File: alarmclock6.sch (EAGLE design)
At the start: 47 parts, among them Q1 FDN360P, T1 2N2222, X1 MKDSN1,5/2-5,08, X2 MKDSN1,5/2-5,08, X3 MKDSN1,5/2-5,08, X4 MKDSN1,5/2-5,08

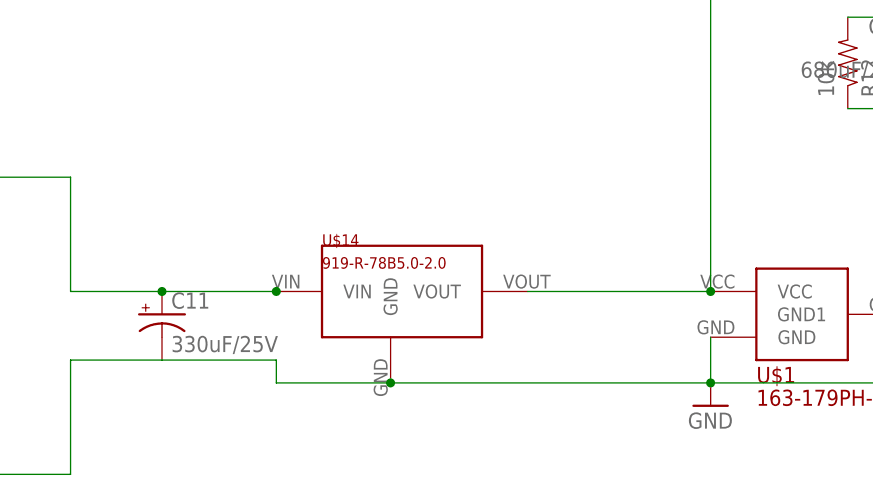
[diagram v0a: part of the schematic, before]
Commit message: bugfix on DC-DC converter
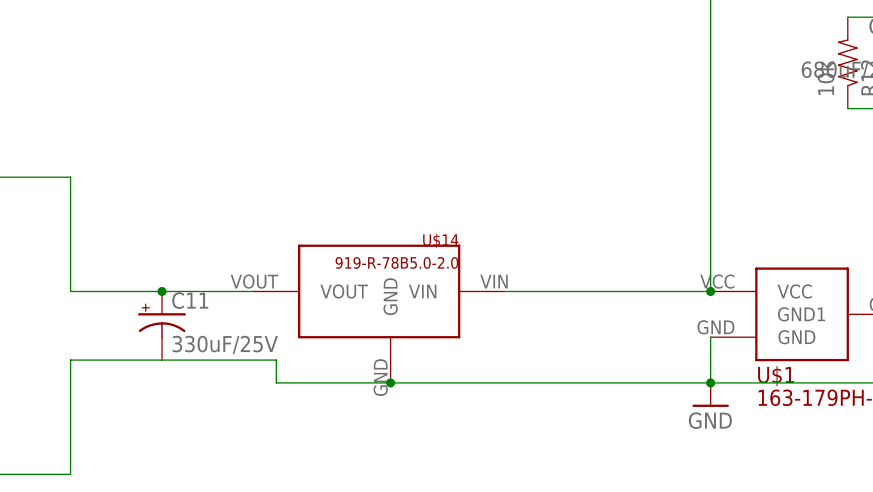
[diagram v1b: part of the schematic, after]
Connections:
- net N$3: now also U$14.VOUT; no longer U$14.VIN
- net N$43: now also U$14.VIN; no longer U$14.VOUT
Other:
- moved on the sheet: U$14
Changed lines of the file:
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@@
 <instance part="C18" gate="G$1" x="114.3" y="48.26"/>
 <instance part="C19" gate="G$1" x="119.38" y="48.26"/>
-<instance part="U$14" gate="G$1" x="-137.16" y="-129.54"/>
+<instance part="U$14" gate="G$1" x="-137.16" y="-129.54" rot="MR0"/>
 </instances>
 <busses>
@@
 <wire x1="-172.72" y1="-129.54" x2="-162.56" y2="-129.54" width="0.1524" layer="91"/>
 <pinref part="U$4" gate="G$1" pin="VCC"/>
-<wire x1="-162.56" y1="-129.54" x2="-149.86" y2="-129.54" width="0.1524" layer="91"/>
 <wire x1="-200.66" y1="-124.46" x2="-200.66" y2="-116.84" width="0.1524" layer="91"/>
 <wire x1="-200.66" y1="-116.84" x2="-172.72" y2="-116.84" width="0.1524" layer="91"/>
 <wire x1="-172.72" y1="-116.84" x2="-172.72" y2="-129.54" width="0.1524" layer="91"/>
 <pinref part="C11" gate="G$1" pin="+"/>
+<pinref part="U$14" gate="G$1" pin="VOUT"/>
+<wire x1="-152.4" y1="-129.54" x2="-162.56" y2="-129.54" width="0.1524" layer="91"/>
 <junction x="-162.56" y="-129.54"/>
-<pinref part="U$14" gate="G$1" pin="VIN"/>
-<junction x="-149.86" y="-129.54"/>
 </segment>
 </net>
@@
 <segment>
 <pinref part="U$1" gate="G$1" pin="VCC"/>
-<wire x1="-101.6" y1="-129.54" x2="-121.92" y2="-129.54" width="0.1524" layer="91"/>
 <wire x1="-101.6" y1="-129.54" x2="-101.6" y2="-76.2" width="0.1524" layer="91"/>
 <pinref part="Q1" gate="G$1" pin="S"/>
@@
 <wire x1="-101.6" y1="-76.2" x2="-53.34" y2="-76.2" width="0.1524" layer="91"/>
 <junction x="-53.34" y="-76.2"/>
+<pinref part="U$14" gate="G$1" pin="VIN"/>
+<wire x1="-124.46" y1="-129.54" x2="-101.6" y2="-129.54" width="0.1524" layer="91"/>
 <junction x="-101.6" y="-129.54"/>
-<pinref part="U$14" gate="G$1" pin="VOUT"/>
-</segment>
-</net>
+</segment>
+</net>
